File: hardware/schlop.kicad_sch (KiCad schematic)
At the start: 43 parts, among them SW1 SW_SPST, SW10 SW_SPST, SW11 SW_SPST, SW12 SW_SPST, SW13 SW_SPST, SW14 SW_SPST, SW15 SW_SPST, SW16 SW_SPST, SW17 SW_SPST, SW18 SW_SPST, SW19 SW_SPST, SW2 SW_SPST, SW20 SW_SPST, SW21 SW_SPST, SW3 SW_SPST, SW4 SW_SPST, SW5 SW_SPST, SW6 SW_SPST, SW7 SW_SPST, SW8 SW_SPST, SW9 SW_SPST

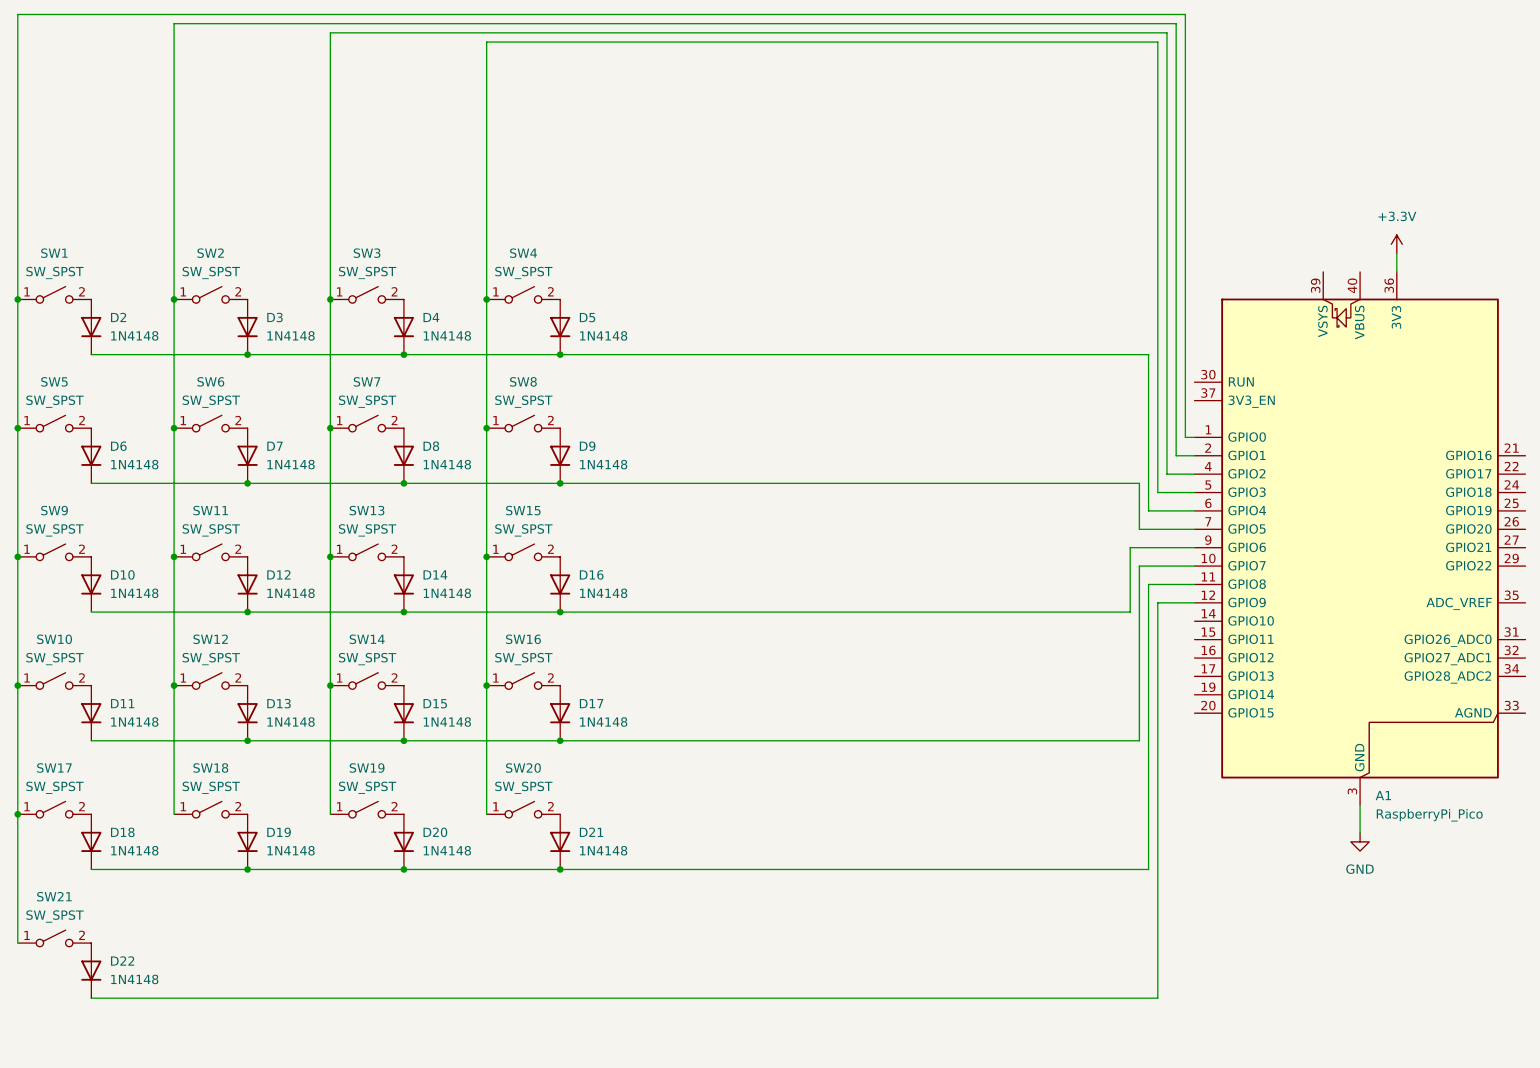
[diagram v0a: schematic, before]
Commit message: finished pcb routing and mounting
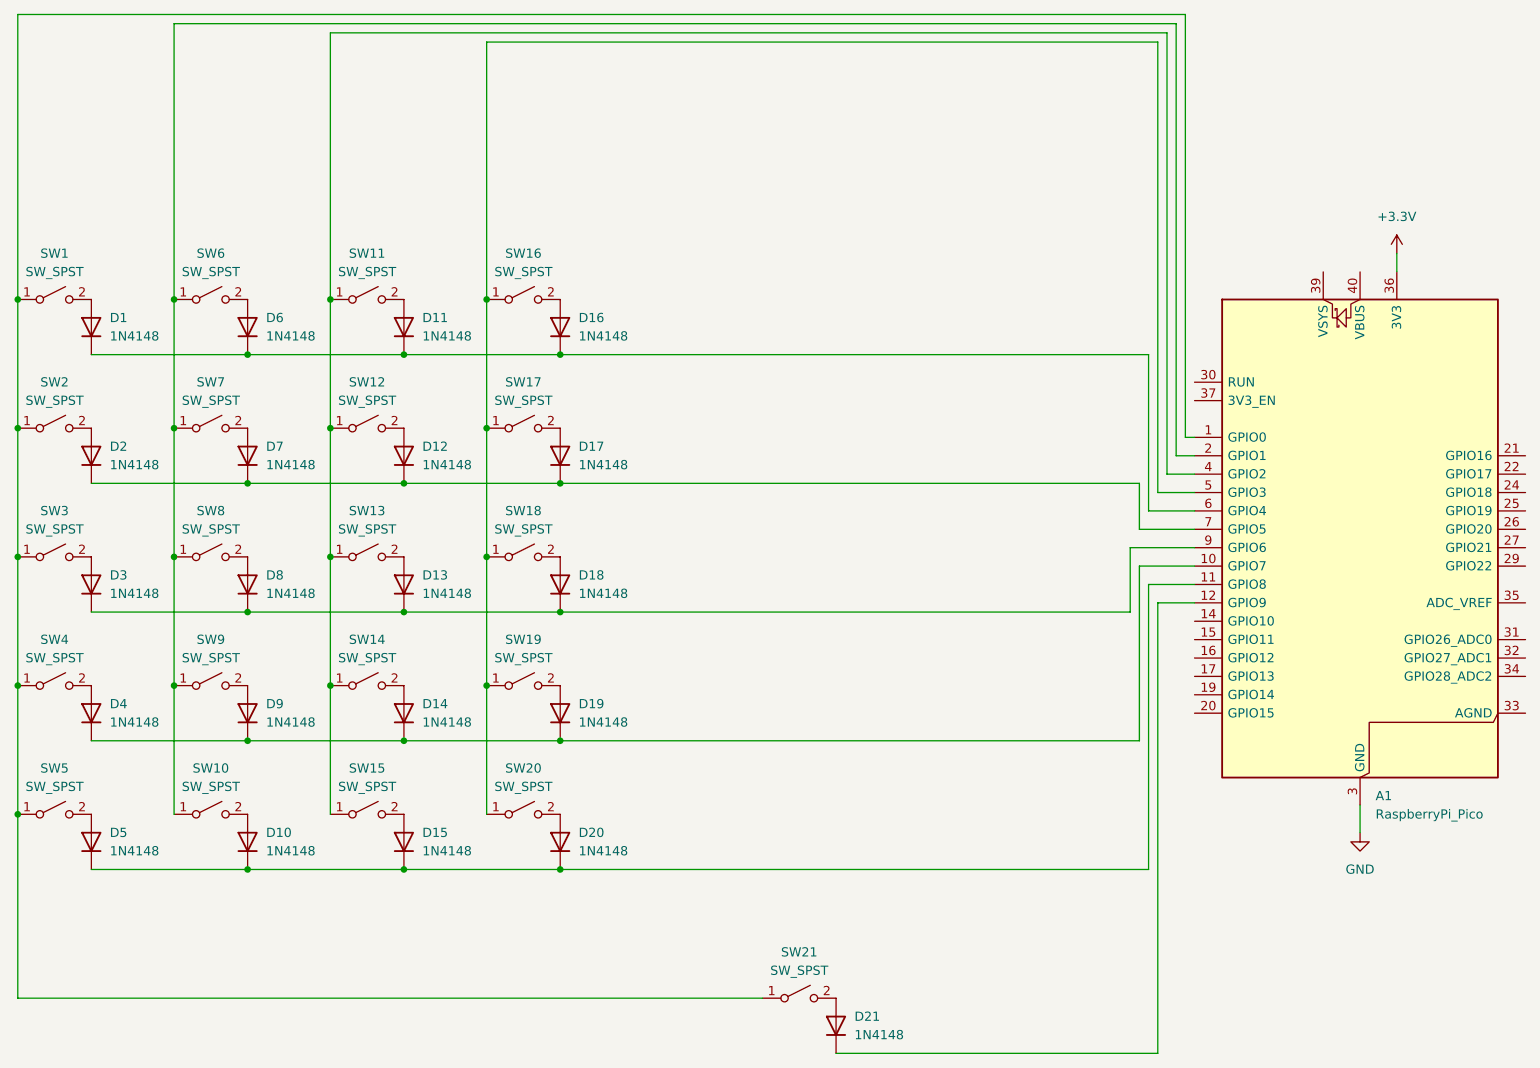
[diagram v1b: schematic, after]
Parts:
- renumbered D2 to D1, D19 to D10, D4 to D11, D8 to D12, D14 to D13, D15 to D14, D20 to D15, D5 to D16, D9 to D17, D16 to D18, D17 to D19, D6 to D2, D21 to D20, D22 to D21, D10 to D3, D11 to D4, D18 to D5, D3 to D6, D12 to D8, D13 to D9, SW18 to SW10, SW3 to SW11, SW7 to SW12, SW19 to SW15, SW4 to SW16, SW8 to SW17, SW15 to SW18, SW16 to SW19, SW5 to SW2, SW9 to SW3, SW10 to SW4, SW17 to SW5, SW2 to SW6, SW6 to SW7, SW11 to SW8, SW12 to SW9
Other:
- moved on the sheet: D21, SW21
